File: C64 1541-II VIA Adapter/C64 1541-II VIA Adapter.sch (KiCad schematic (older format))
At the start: 3 parts, among them J2 SpeedDOS, U1 6522

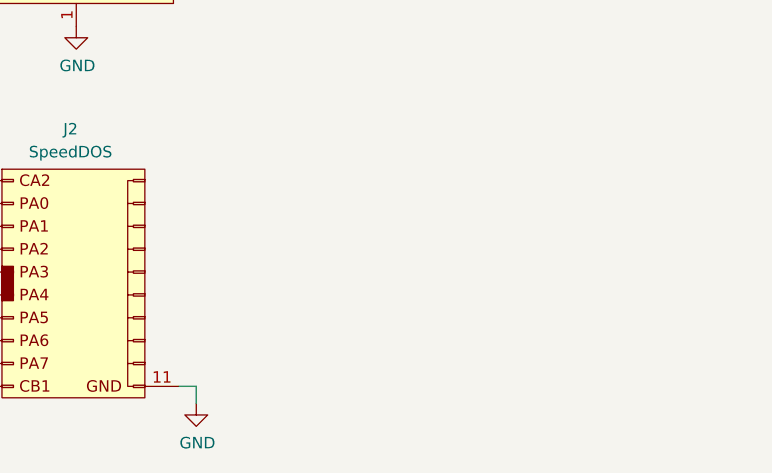
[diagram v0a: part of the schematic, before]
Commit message: User port adapter added
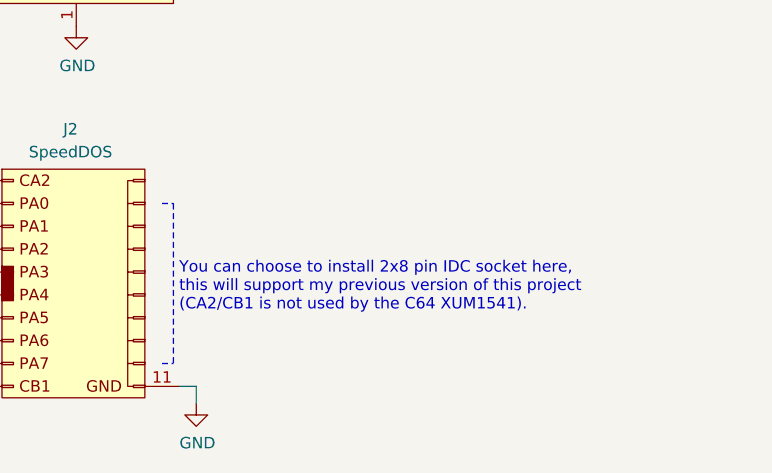
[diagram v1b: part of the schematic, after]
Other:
- note added: "You can choose to install 2x8 pin IDC socket here,\nthis will support my previous version of this project\n(CA2/CB1 is not used by the C64 XUM1541)."
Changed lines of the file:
@@
 Wire Wire Line
 	6225 5625 6750 5625
+Text Notes 7675 5300 0    50   ~ 0
+You can choose to install 2x8 pin IDC socket here,\nthis will support my previous version of this project\n(CA2/CB1 is not used by the C64 XUM1541).
+Wire Notes Line
+	7600 5525 7650 5525
+Wire Notes Line
+	7600 4825 7650 4825
+Wire Notes Line
+	7650 4825 7650 5525
 Wire Bus Line
 	3650 1275 3650 3750

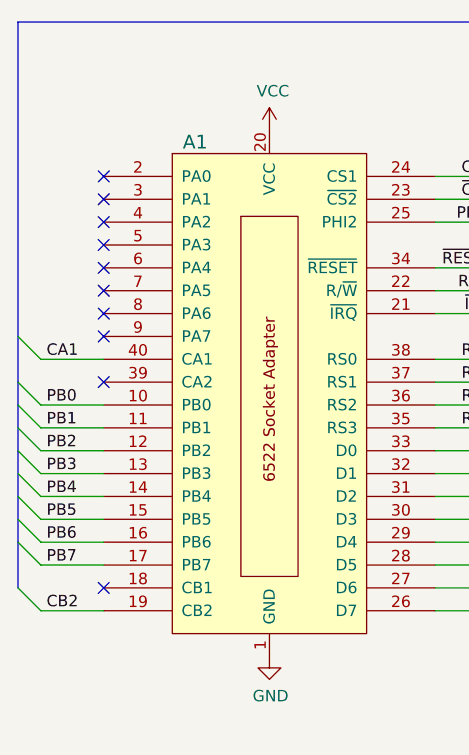
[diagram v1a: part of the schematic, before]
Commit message: Link remaining pins
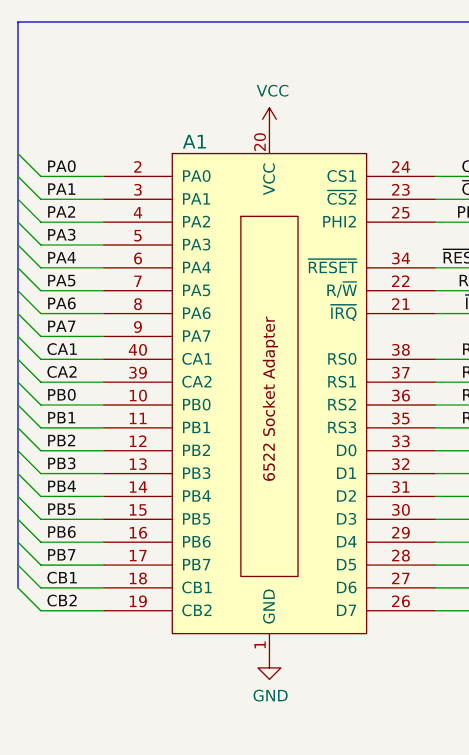
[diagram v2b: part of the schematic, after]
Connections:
- net CA2: now also A1.39 (CA2)
- net CB1: now also A1.18 (CB1)
- net PA0: now also A1.2 (PA0)
- net PA1: now also A1.3 (PA1)
- net PA2: now also A1.4 (PA2)
- net PA3: now also A1.5 (PA3)
- net PA4: now also A1.6 (PA4)
- net PA5: now also A1.7 (PA5)
- net PA6: now also A1.8 (PA6)
- net PA7: now also A1.9 (PA7)
- no-connect marks 10 -> 0
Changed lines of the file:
@@
 Text Label 6250 5625 0    50   ~ 0
 CB1
-NoConn ~ 4025 1950
-NoConn ~ 4025 2050
-NoConn ~ 4025 2150
-NoConn ~ 4025 2250
-NoConn ~ 4025 2350
-NoConn ~ 4025 2450
-NoConn ~ 4025 2550
-NoConn ~ 4025 2650
-NoConn ~ 4025 3750
-NoConn ~ 4025 2850
 Entry Wire Line
 	5750 2350 5850 2250
@@
 PA7
 Entry Wire Line
-	6225 2850 6125 2750
-Text Label 6250 2850 0    50   ~ 0
-CA2
-Entry Wire Line
 	6225 3750 6125 3650
 Text Label 6250 3750 0    50   ~ 0
 CB1
 Wire Wire Line
-	6225 2850 6500 2850
-Wire Wire Line
 	6225 1950 6500 1950
 Wire Wire Line
@@
 Text Label 6250 2750 0    50   ~ 0
 CA1
-Entry Wire Line
-	6225 2950 6125 2850
 Wire Wire Line
 	6225 2950 6500 2950
@@
 Wire Notes Line
 	7650 4825 7650 5525
+Entry Wire Line
+	3750 2250 3650 2150
+Entry Wire Line
+	3750 2150 3650 2050
+Entry Wire Line
+	3750 2050 3650 1950
+Entry Wire Line
+	3750 1950 3650 1850
+Entry Wire Line
+	3650 2250 3750 2350
+Entry Wire Line
+	3650 2350 3750 2450
+Entry Wire Line
+	3650 2450 3750 2550
+Entry Wire Line
+	3650 2550 3750 2650
+Text Label 3775 1950 0    50   ~ 0
+PA0
+Text Label 3775 2050 0    50   ~ 0
+PA1
+Text Label 3775 2150 0    50   ~ 0
+PA2
+Text Label 3775 2250 0    50   ~ 0
+PA3
+Text Label 3775 2350 0    50   ~ 0
+PA4
+Text Label 3775 2450 0    50   ~ 0
+PA5
+Text Label 3775 2550 0    50   ~ 0
+PA6
+Text Label 3775 2650 0    50   ~ 0
+PA7
+Wire Wire Line
+	3750 1950 4025 1950
+Wire Wire Line
+	3750 2050 4025 2050
+Wire Wire Line
+	3750 2150 4025 2150
+Wire Wire Line
+	3750 2250 4025 2250
+Wire Wire Line
+	3750 2350 4025 2350
+Wire Wire Line
+	3750 2450 4025 2450
+Wire Wire Line
+	3750 2550 4025 2550
+Wire Wire Line
+	3750 2650 4025 2650
+Entry Wire Line
+	6225 2850 6125 2750
+Text Label 6250 2850 0    50   ~ 0
+CA2
+Wire Wire Line
+	6225 2850 6500 2850
+Entry Wire Line
+	6225 2950 6125 2850
+Entry Wire Line
+	3750 2850 3650 2750
+Text Label 3775 2850 0    50   ~ 0
+CA2
+Wire Wire Line
+	3750 2850 4025 2850
+Entry Wire Line
+	3750 3750 3650 3650
+Text Label 3775 3750 0    50   ~ 0
+CB1
+Wire Wire Line
+	3750 3750 4025 3750
 Wire Bus Line
 	3650 1275 3650 3750

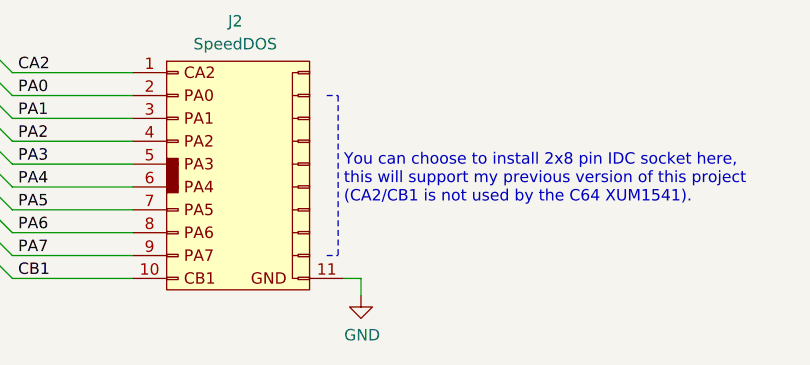
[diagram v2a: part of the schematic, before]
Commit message: Added GND jumper
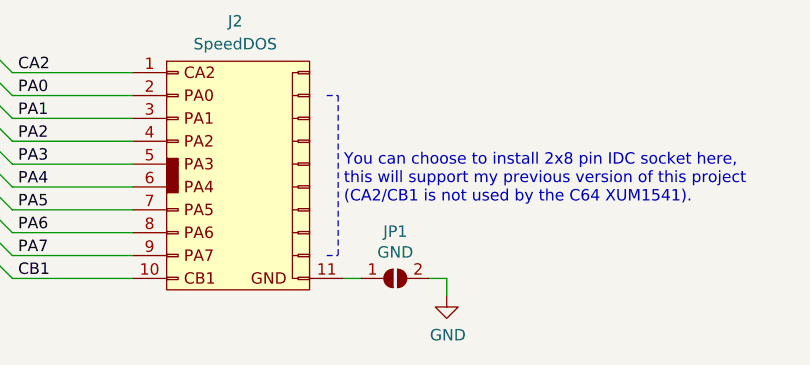
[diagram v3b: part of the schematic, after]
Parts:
- added JP1: GND, solder_bridge:bridge_r, symbol Jumper:SolderJumper_2_Open
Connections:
- net GND: now also JP1.2 (B); no longer J2.11 (Pin_11)
- new net: J2.11 (Pin_11), JP1.1 (A)
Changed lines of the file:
@@
 L power:GND #PWR01
 U 1 1 5EF2A7F5
-P 7750 5700
-F 0 "#PWR01" H 7750 5450 50  0001 C CNN
-F 1 "GND" H 7755 5527 50  0000 C CNN
-F 2 "" H 7750 5700 50  0001 C CNN
-F 3 "" H 7750 5700 50  0001 C CNN
-	1    7750 5700
-	1    0    0    -1
-$EndComp
-Wire Wire Line
-	7675 5625 7750 5625
-Wire Wire Line
-	7750 5625 7750 5700
+P 8125 5700
+F 0 "#PWR01" H 8125 5450 50  0001 C CNN
+F 1 "GND" H 8130 5527 50  0000 C CNN
+F 2 "" H 8125 5700 50  0001 C CNN
+F 3 "" H 8125 5700 50  0001 C CNN
+	1    8125 5700
+	1    0    0    -1
+$EndComp
+Wire Wire Line
+	8050 5625 8125 5625
+Wire Wire Line
+	8125 5625 8125 5700
 $Comp
 L 6522:6522 U1
@@
 Wire Wire Line
 	3750 3750 4025 3750
+$Comp
+L Jumper:SolderJumper_2_Open JP1
+U 1 1 6090AA6A
+P 7900 5625
+F 0 "JP1" H 7900 5830 50  0000 C CNN
+F 1 "GND" H 7900 5739 50  0000 C CNN
+F 2 "solder_bridge:bridge_r" H 7900 5625 50  0001 C CNN
+F 3 "~" H 7900 5625 50  0001 C CNN
+	1    7900 5625
+	1    0    0    -1
+$EndComp
+Wire Wire Line
+	7675 5625 7750 5625
 Wire Bus Line
 	3650 1275 3650 3750
